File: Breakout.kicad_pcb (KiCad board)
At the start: 2 copper layers, 30 x 33 mm, 6 parts, among them J1 Breakout, U1 MCP2518FDT-H/SL, Y1 4 MHz

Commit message: cleaned up
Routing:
- net Net-(J1-Pad11): track 38.2 -> 37.3 mm
- net Net-(J1-Pad10): track 31.1 -> 30.2 mm
- net Net-(J1-Pad9): track 28.0 -> 28.6 mm
- net Net-(J1-Pad8): track 22.8 -> 22.3 mm
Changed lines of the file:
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@@
   (segment (start 163.5 97) (end 164.5 98) (width 0.25) (layer "F.Cu") (net 7))
   (segment (start 163.5 94.5) (end 163.5 97) (width 0.25) (layer "F.Cu") (net 7))
+  (segment (start 164.378198 94.378198) (end 164.378198 96.52) (width 0.25) (layer "F.Cu") (net 8))
+  (segment (start 161.51 91.51) (end 164.378198 94.378198) (width 0.25) (layer "F.Cu") (net 8))
+  (segment (start 171.5 96.29) (end 171.5 93.29) (width 0.25) (layer "F.Cu") (net 8))
   (segment (start 171.5 93.29) (end 172 92.79) (width 0.25) (layer "F.Cu") (net 8))
+  (segment (start 160.7825 91.51) (end 161.51 91.51) (width 0.25) (layer "F.Cu") (net 8))
+  (segment (start 165.1 97.241802) (end 170.548198 97.241802) (width 0.25) (layer "F.Cu") (net 8))
+  (segment (start 164.378198 96.52) (end 165.1 97.241802) (width 0.25) (layer "F.Cu") (net 8))
   (segment (start 172 92.79) (end 173.75 92.79) (width 0.25) (layer "F.Cu") (net 8))
-  (segment (start 160.7825 91.51) (end 161.51 91.51) (width 0.25) (layer "F.Cu") (net 8))
-  (segment (start 164.5 97) (end 170.79 97) (width 0.25) (layer "F.Cu") (net 8))
-  (segment (start 170.79 97) (end 171.5 96.29) (width 0.25) (layer "F.Cu") (net 8))
-  (segment (start 171.5 96.29) (end 171.5 93.29) (width 0.25) (layer "F.Cu") (net 8))
-  (segment (start 164.5 94.5) (end 164.5 97) (width 0.25) (layer "F.Cu") (net 8))
-  (segment (start 161.51 91.51) (end 164.5 94.5) (width 0.25) (layer "F.Cu") (net 8))
-  (segment (start 165.5 96.25) (end 169.71 96.25) (width 0.25) (layer "F.Cu") (net 9))
-  (segment (start 165.5 94.25) (end 165.5 96.25) (width 0.25) (layer "F.Cu") (net 9))
-  (segment (start 161.49 90.24) (end 165.5 94.25) (width 0.25) (layer "F.Cu") (net 9))
+  (segment (start 170.548198 97.241802) (end 171.5 96.29) (width 0.25) (layer "F.Cu") (net 8))
+  (segment (start 160.7825 90.24) (end 161.49 90.24) (width 0.25) (layer "F.Cu") (net 9))
+  (segment (start 165.25 94) (end 165.25 96.25) (width 0.25) (layer "F.Cu") (net 9))
   (segment (start 172.54 90.25) (end 173.75 90.25) (width 0.25) (layer "F.Cu") (net 9))
   (segment (start 171 94.96) (end 171 91.79) (width 0.25) (layer "F.Cu") (net 9))
-  (segment (start 160.7825 90.24) (end 161.49 90.24) (width 0.25) (layer "F.Cu") (net 9))
+  (segment (start 165.25 96.25) (end 165.52 96.52) (width 0.25) (layer "F.Cu") (net 9))
+  (segment (start 165.52 96.52) (end 169.44 96.52) (width 0.25) (layer "F.Cu") (net 9))
+  (segment (start 161.49 90.24) (end 165.25 94) (width 0.25) (layer "F.Cu") (net 9))
   (segment (start 171 91.79) (end 172.54 90.25) (width 0.25) (layer "F.Cu") (net 9))
-  (segment (start 169.71 96.25) (end 171 94.96) (width 0.25) (layer "F.Cu") (net 9))
+  (segment (start 169.44 96.52) (end 171 94.96) (width 0.25) (layer "F.Cu") (net 9))
+  (segment (start 165.7 93.4325) (end 165.7 95.42) (width 0.25) (layer "F.Cu") (net 10))
+  (segment (start 166.03 95.75) (end 169.5 95.75) (width 0.25) (layer "F.Cu") (net 10))
+  (segment (start 170 95.25) (end 170 92) (width 0.25) (layer "F.Cu") (net 10))
+  (segment (start 170 92) (end 170.75 91.25) (width 0.25) (layer "F.Cu") (net 10))
   (segment (start 170.75 91.25) (end 170.75 90.71) (width 0.25) (layer "F.Cu") (net 10))
-  (segment (start 170 92) (end 170.75 91.25) (width 0.25) (layer "F.Cu") (net 10))
+  (segment (start 165.7 95.42) (end 166.03 95.75) (width 0.25) (layer "F.Cu") (net 10))
   (segment (start 160.7825 88.97) (end 161.2375 88.97) (width 0.25) (layer "F.Cu") (net 10))
-  (segment (start 165.95 95.75) (end 169.5 95.75) (width 0.25) (layer "F.Cu") (net 10))
+  (segment (start 161.2375 88.97) (end 165.7 93.4325) (width 0.25) (layer "F.Cu") (net 10))
+  (segment (start 170.75 90.71) (end 173.75 87.71) (width 0.25) (layer "F.Cu") (net 10))
   (segment (start 169.5 95.75) (end 170 95.25) (width 0.25) (layer "F.Cu") (net 10))
-  (segment (start 161.2375 88.97) (end 165.95 93.6825) (width 0.25) (layer "F.Cu") (net 10))
-  (segment (start 170.75 90.71) (end 173.75 87.71) (width 0.25) (layer "F.Cu") (net 10))
-  (segment (start 170 95.25) (end 170 92) (width 0.25) (layer "F.Cu") (net 10))
-  (segment (start 165.95 93.6825) (end 165.95 95.75) (width 0.25) (layer "F.Cu") (net 10))
+  (segment (start 159.75 86.75) (end 161.75 86.75) (width 0.25) (layer "F.Cu") (net 11))
+  (segment (start 161.75 86.75) (end 164 89) (width 0.25) (layer "F.Cu") (net 11))
   (segment (start 155.3825 87.7) (end 158.8 87.7) (width 0.25) (layer "F.Cu") (net 11))
-  (segment (start 161.75 86.75) (end 164 89) (width 0.25) (layer "F.Cu") (net 11))
-  (segment (start 168.25 88.13) (end 173.75 82.63) (width 0.25) (layer "F.Cu") (net 11))
+  (segment (start 164 89) (end 167.38 89) (width 0.25) (layer "F.Cu") (net 11))
   (segment (start 158.8 87.7) (end 159.75 86.75) (width 0.25) (layer "F.Cu") (net 11))
-  (segment (start 159.75 86.75) (end 161.75 86.75) (width 0.25) (layer "F.Cu") (net 11))
-  (segment (start 168.25 89) (end 168.25 88.13) (width 0.25) (layer "F.Cu") (net 11))
-  (segment (start 164 89) (end 168.25 89) (width 0.25) (layer "F.Cu") (net 11))
-  (segment (start 153.75 87.25) (end 155 86) (width 0.25) (layer "F.Cu") (net 12))
-  (segment (start 153.75 89) (end 153.75 87.25) (width 0.25) (layer "F.Cu") (net 12))
-  (segment (start 155.3825 88.97) (end 153.78 88.97) (width 0.25) (layer "F.Cu") (net 12))
+  (segment (start 167.38 89) (end 173.75 82.63) (width 0.25) (layer "F.Cu") (net 11))
+  (segment (start 155.3825 88.97) (end 153.456396 88.97) (width 0.25) (layer "F.Cu") (net 12))
+  (segment (start 155 86) (end 167.67 86) (width 0.25) (layer "F.Cu") (net 12))
+  (segment (start 167.8 85.87) (end 168.92 84.75) (width 0.25) (layer "F.Cu") (net 12))
+  (segment (start 153.25 88.763604) (end 153.25 87.75) (width 0.25) (layer "F.Cu") (net 12))
+  (segment (start 153.456396 88.97) (end 153.25 88.763604) (width 0.25) (layer "F.Cu") (net 12))
+  (segment (start 153.25 87.75) (end 155 86) (width 0.25) (layer "F.Cu") (net 12))
+  (segment (start 168.92 84.75) (end 173.75 79.92) (width 0.25) (layer "F.Cu") (net 12))
   (segment (start 167.67 86) (end 168.92 84.75) (width 0.25) (layer "F.Cu") (net 12))
-  (segment (start 167.8 85.87) (end 168.92 84.75) (width 0.25) (layer "F.Cu") (net 12))
-  (segment (start 153.78 88.97) (end 153.75 89) (width 0.25) (layer "F.Cu") (net 12))
-  (segment (start 168.92 84.75) (end 173.75 79.92) (width 0.25) (layer "F.Cu") (net 12))
-  (segment (start 155 86) (end 167.67 86) (width 0.25) (layer "F.Cu") (net 12))
-  (segment (start 167 85) (end 167 84.3) (width 0.25) (layer "F.Cu") (net 13))
-  (segment (start 167 84.3) (end 173.75 77.55) (width 0.25) (layer "F.Cu") (net 13))
-  (segment (start 155.3825 90.24) (end 152.75 90.24) (width 0.25) (layer "F.Cu") (net 13))
-  (segment (start 152.75 90.24) (end 152.75 87.25) (width 0.25) (layer "F.Cu") (net 13))
-  (segment (start 155 85) (end 167 85) (width 0.25) (layer "F.Cu") (net 13))
+  (segment (start 153.5775 90.24) (end 152.75 89.4125) (width 0.25) (layer "F.Cu") (net 13))
+  (segment (start 155 85) (end 166.46 85) (width 0.25) (layer "F.Cu") (net 13))
   (segment (start 152.75 87.25) (end 155 85) (width 0.25) (layer "F.Cu") (net 13))
-  (segment (start 170 79.75) (end 170 75.75) (width 0.25) (layer "F.Cu") (net 14))
+  (segment (start 155.3825 90.24) (end 153.5775 90.24) (width 0.25) (layer "F.Cu") (net 13))
+  (segment (start 166.46 85) (end 173.75 77.71) (width 0.25) (layer "F.Cu") (net 13))
+  (segment (start 152.75 89.4125) (end 152.75 87.25) (width 0.25) (layer "F.Cu") (net 13))
+  (segment (start 173.75 77.71) (end 173.75 77.55) (width 0.25) (layer "F.Cu") (net 13))
+  (segment (start 155.3825 91.51) (end 152.47 91.51) (width 0.25) (layer "F.Cu") (net 14))
+  (segment (start 154 84) (end 165.75 84) (width 0.25) (layer "F.Cu") (net 14))
   (segment (start 170.74 75.01) (end 173.75 75.01) (width 0.25) (layer "F.Cu") (net 14))
-  (segment (start 154 84) (end 165.75 84) (width 0.25) (layer "F.Cu") (net 14))
-  (segment (start 155.3825 91.51) (end 154.01 91.51) (width 0.25) (layer "F.Cu") (net 14))
   (segment (start 165.75 84) (end 170 79.75) (width 0.25) (layer "F.Cu") (net 14))
   (segment (start 152 86) (end 154 84) (width 0.25) (layer "F.Cu") (net 14))
-  (segment (start 153.52 92) (end 152 92) (width 0.25) (layer "F.Cu") (net 14))
-  (segment (start 154.01 91.51) (end 153.52 92) (width 0.25) (layer "F.Cu") (net 14))
+  (segment (start 152 91.04) (end 152 86) (width 0.25) (layer "F.Cu") (net 14))
+  (segment (start 152.47 91.51) (end 152 91.04) (width 0.25) (layer "F.Cu") (net 14))
   (segment (start 170 75.75) (end 170.74 75.01) (width 0.25) (layer "F.Cu") (net 14))
-  (segment (start 152 92) (end 152 86) (width 0.25) (layer "F.Cu") (net 14))
+  (segment (start 170 79.75) (end 170 75.75) (width 0.25) (layer "F.Cu") (net 14))
   (zone (net 1) (net_name "GND") (layer "F.Cu") (hatch edge 0.508)
     (connect_pads (clearance 0.508))

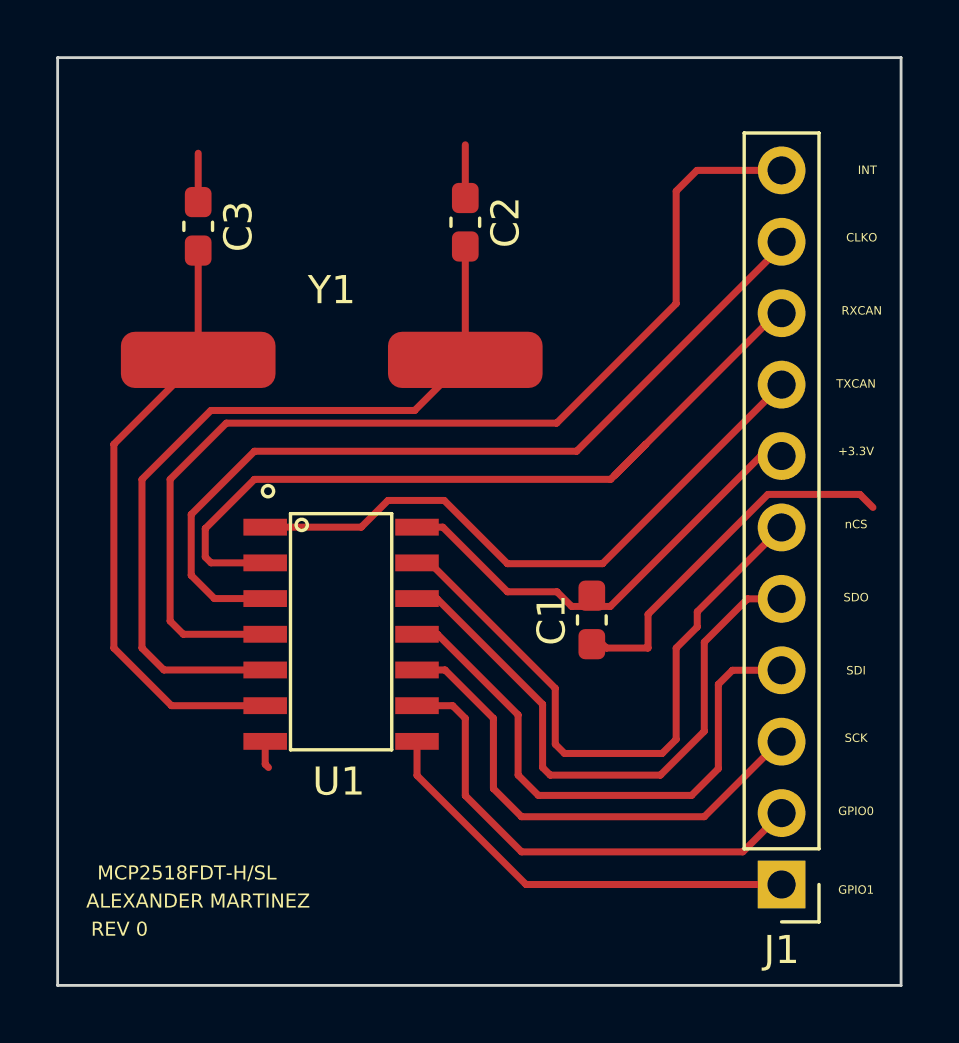
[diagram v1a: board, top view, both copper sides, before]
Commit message: cleaned ground
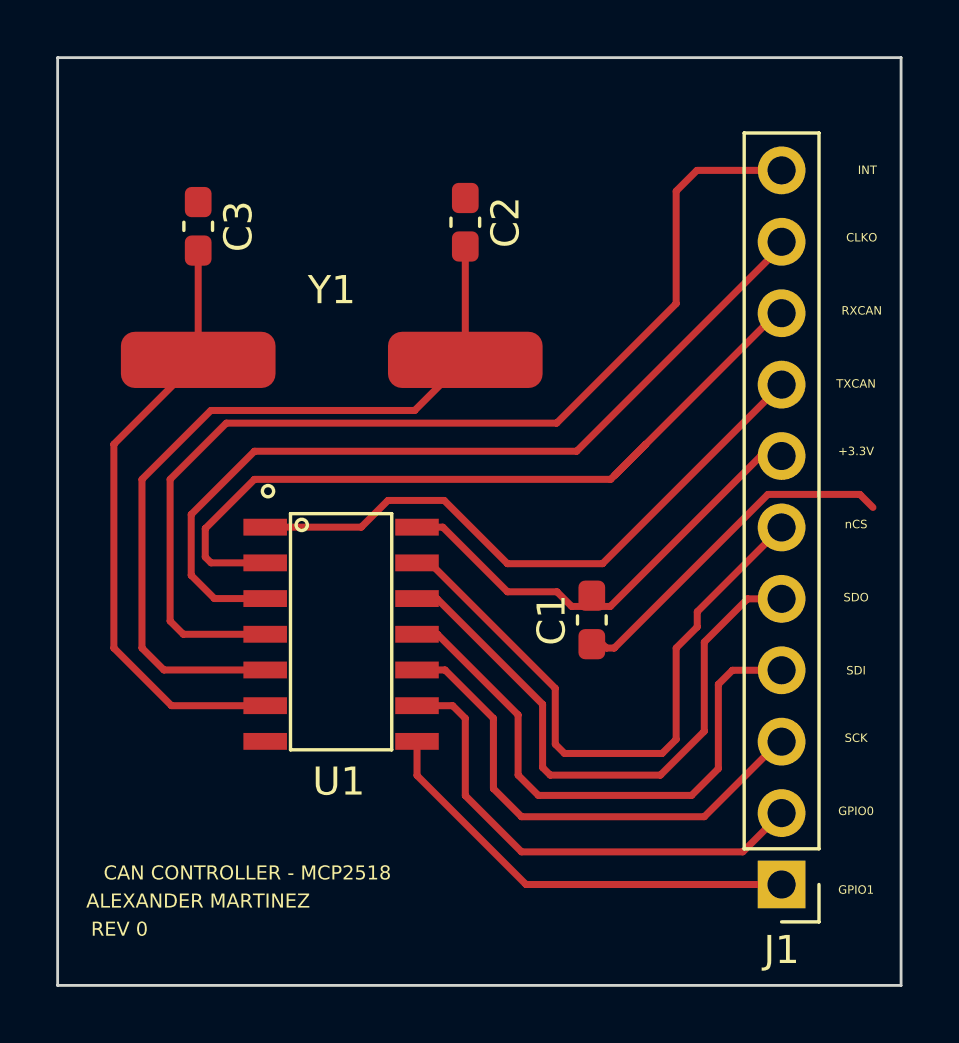
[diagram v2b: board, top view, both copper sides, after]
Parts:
- U1: value MCP2518FDT-H/SL -> CAN CONTROLLER - MCP2518
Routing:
- net GND: track 18.5 -> 12.8 mm
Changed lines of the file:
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@@
       (effects (font (size 1 1) (thickness 0.15)))
     )
-    (fp_text value "MCP2518FDT-H/SL" (at 8.82 12.5825 unlocked) (layer "F.SilkS")
+    (fp_text value "CAN CONTROLLER - MCP2518" (at 8.82 10.4325 unlocked) (layer "F.SilkS")
       (effects (font (size 0.5 0.5) (thickness 0.125)))
     )
@@
     (effects (font (size 0.3 0.3) (thickness 0.06)))
   )
-  (segment (start 162.5 76.375) (end 162.5 74.1) (width 0.25) (layer "F.Cu") (net 1))
-  (segment (start 155.3825 96.1325) (end 155.5 96.25) (width 0.25) (layer "F.Cu") (net 1))
-  (segment (start 169 92) (end 167.52 92) (width 0.25) (layer "F.Cu") (net 1))
-  (segment (start 153 76.1375) (end 153 74.4) (width 0.25) (layer "F.Cu") (net 1))
   (segment (start 167.52 92) (end 167 91.48) (width 0.25) (layer "F.Cu") (net 1))
+  (segment (start 177 87) (end 176.535 86.535) (width 0.25) (layer "F.Cu") (net 1))
+  (segment (start 167.798299 92) (end 167.52 92) (width 0.25) (layer "F.Cu") (net 1))
+  (segment (start 173.263299 86.535) (end 167.798299 92) (width 0.25) (layer "F.Cu") (net 1))
+  (segment (start 176.535 86.535) (end 173.263299 86.535) (width 0.25) (layer "F.Cu") (net 1))
   (segment (start 153 76.17) (end 153 76) (width 0.25) (layer "F.Cu") (net 1))
-  (segment (start 176.535 86.535) (end 173.263299 86.535) (width 0.25) (layer "F.Cu") (net 1))
-  (segment (start 155.3825 95.32) (end 155.3825 96.1325) (width 0.25) (layer "F.Cu") (net 1))
-  (segment (start 173.263299 86.535) (end 169 90.798299) (width 0.25) (layer "F.Cu") (net 1))
-  (segment (start 169 90.798299) (end 169 92) (width 0.25) (layer "F.Cu") (net 1))
-  (segment (start 177 87) (end 176.535 86.535) (width 0.25) (layer "F.Cu") (net 1))
   (segment (start 165.762391 90) (end 166.282391 90.52) (width 0.25) (layer "F.Cu") (net 2))
   (segment (start 173.00761 85.17) (end 173.75 85.17) (width 0.25) (layer "F.Cu") (net 2))
